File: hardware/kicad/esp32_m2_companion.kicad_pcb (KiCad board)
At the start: 4 copper layers, 22 x 42 mm, 33 parts, among them J1 M2_KEYB_2242_EDGE, J3 Conn_01x04, J4 Conn_01x08, U1 USBLC6-2SC6, U2 ESP32-S3-WROOM-1

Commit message: leds: simple 3D model for the side-view LED (D3); link D3/D4 to their library
- 3dmodels/LED_TJ-S1706_SideView.wrl: 1.70x0.60x1.10 mm body, lens on
  the emitting face, end terminals (renders showed bare pads).
- D3/D4 board instances had no library nickname, so DRC library parity
  never checked them (corrects an earlier claim, see findings). Linked
  to esp32_m2_companion:LED_TJ-S1706_SideView; parity passes.

make drc: 0 violations, 0 unconnected.

Co-Authored-By: Claude Opus 5.5 <noreply@anthropic.com>
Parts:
- D3, D4: footprint LED_TJ-S1706_SideView -> esp32_m2_companion:LED_TJ-S1706_SideView
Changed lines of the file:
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@@
 		)
 	)
-	(footprint "LED_TJ-S1706_SideView"
+	(footprint "esp32_m2_companion:LED_TJ-S1706_SideView"
 		(layer "B.Cu")
 		(at 90.2 126.4 90)
@@
 		)
 		(embedded_fonts no)
+		(model "${KIPRJMOD}/3dmodels/LED_TJ-S1706_SideView.wrl"
+			(offset
+				(xyz 0 0 0)
+			)
+			(scale
+				(xyz 1 1 1)
+			)
+			(rotate
+				(xyz 0 0 0)
+			)
+		)
 	)
 	(footprint "TestPoint:TestPoint_Pad_D1.5mm"
@@
 		(embedded_fonts no)
 	)
-	(footprint "LED_TJ-S1706_SideView"
+	(footprint "esp32_m2_companion:LED_TJ-S1706_SideView"
 		(layer "B.Cu")
 		(at 90.2 129.8 90)
@@
 		)
 		(embedded_fonts no)
+		(model "${KIPRJMOD}/3dmodels/LED_TJ-S1706_SideView.wrl"
+			(offset
+				(xyz 0 0 0)
+			)
+			(scale
+				(xyz 1 1 1)
+			)
+			(rotate
+				(xyz 0 0 0)
+			)
+		)
 	)
 	(footprint "Resistor_SMD:R_0603_1608Metric"

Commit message: v2 GATE V3 (wip): RPW eFuse footprint, netlist->board sync keeping rev-B routing
- tools/gen_fp_rpw.py: TI RPW0010A footprint from tps25947.pdf drawing
  4225183/A (land p.73, stencil p.74: split paste on IN/OUT, L-pads as
  two rects per pin), NSMD 0.05 mm.
- tools/v2_sync_pcb.py: KiCad-9 headless 'update PCB from netlist' in two
  processes (remove changed footprints; add new ones parked off-card and
  assign every pad net from the netlist). Applied: FB1 0805->0603, 31 new
  footprints, 167 pad nets set, no existing net changed.

Co-Authored-By: Claude Opus 5.5 <noreply@anthropic.com>
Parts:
- added C10: 100nF 50V, Capacitor_SMD:C_0603_1608Metric, F.Cu at (118.0, 108.0)
- added C11: 100nF 50V, Capacitor_SMD:C_0603_1608Metric, F.Cu at (118.0, 111.0)
- added C12: 100nF 50V, Capacitor_SMD:C_0603_1608Metric, F.Cu at (118.0, 114.0)
- added C13: 1uF 50V, Capacitor_SMD:C_0603_1608Metric, F.Cu at (118.0, 117.0)
- added C14: 100nF 50V, Capacitor_SMD:C_0603_1608Metric, F.Cu at (118.0, 120.0)
- added Q1: SSM6N56FE, Package_TO_SOT_SMD:SOT-563, F.Cu at (118.0, 126.0)
- added Q2: SSM6N56FE, Package_TO_SOT_SMD:SOT-563, F.Cu at (118.0, 129.0)
- added Q3: SSM6N56FE, Package_TO_SOT_SMD:SOT-563, F.Cu at (118.0, 132.0)
- added R20: 4k7, Resistor_SMD:R_0402_1005Metric, F.Cu at (118.0, 135.0)
- added R21: 4k7, Resistor_SMD:R_0402_1005Metric, F.Cu at (118.0, 138.0)
- added R22: 1M, Resistor_SMD:R_0402_1005Metric, F.Cu at (118.0, 141.0)
- added R23: 1M, Resistor_SMD:R_0402_1005Metric, F.Cu at (118.0, 144.0)
- added R24: 100k, Resistor_SMD:R_0402_1005Metric, F.Cu at (118.0, 147.0)
- added R25: 100k, Resistor_SMD:R_0402_1005Metric, F.Cu at (118.0, 150.0)
- added R26: 10k, Resistor_SMD:R_0603_1608Metric, F.Cu at (118.0, 153.0)
- added R27: 100k, Resistor_SMD:R_0402_1005Metric, F.Cu at (118.0, 156.0)
- added R28: 100k, Resistor_SMD:R_0402_1005Metric, F.Cu at (118.0, 159.0)
- added R29: 1M, Resistor_SMD:R_0402_1005Metric, F.Cu at (118.0, 162.0)
- added R30: 10k, Resistor_SMD:R_0603_1608Metric, F.Cu at (118.0, 165.0)
- added R31: 100k 0.1%, Resistor_SMD:R_0402_1005Metric, F.Cu at (118.0, 168.0)
- added R32: 52.3k 0.1%, Resistor_SMD:R_0402_1005Metric, F.Cu at (118.0, 171.0)
- added R33: 1M, Resistor_SMD:R_0402_1005Metric, F.Cu at (118.0, 174.0)
- added R34: 3.3k, Resistor_SMD:R_0402_1005Metric, F.Cu at (118.0, 177.0)
- added RN1: 220R, Resistor_SMD:R_Array_Convex_4x0402, F.Cu at (118.0, 180.0)
- added RN2: 220R, Resistor_SMD:R_Array_Convex_4x0402, F.Cu at (118.0, 183.0)
- added RN3: 220R, Resistor_SMD:R_Array_Convex_4x0402, F.Cu at (118.0, 186.0)
- added U3: TMUX1511_RSV, Package_DFN_QFN:UQFN-16_1.8x2.6mm_P0.4mm, F.Cu at (118.0, 189.0)
- added U4: TMUX1511_RSV, Package_DFN_QFN:UQFN-16_1.8x2.6mm_P0.4mm, F.Cu at (118.0, 192.0)
- added U5: TMUX1511_RSV, Package_DFN_QFN:UQFN-16_1.8x2.6mm_P0.4mm, F.Cu at (118.0, 195.0)
- added U6: TPS259470A_RPW, esp32_m2_companion:TI_RPW_VQFN-10_2x2mm_P0.5mm, F.Cu at (118.0, 198.0)
- FB1: value 100R@100MHz 800mA -> 120R@100MHz 2A; footprint Inductor_SMD:L_0805_2012Metric -> Inductor_SMD:L_0603_1608Metric; moved to F.Cu
- moved FB1 33.5 mm to (118.0, 123.0), turned to 0 degrees
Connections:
- FB1 pad 1: +3V3_M2 -> +3V3_EFUSE
- J1 pad 1: (no net) -> CONFIG_3
- J1 pad 10: (no net) -> LED_1_n
- J1 pad 21: (no net) -> GND
- J1 pad 23: (no net) -> WAKE_ON_WWAN_n
- J1 pad 26: (no net) -> W_DISABLE2_n
- J1 pad 30: (no net) -> EXP_0
- J1 pad 32: (no net) -> EXP_1
- J1 pad 34: (no net) -> EXP_2
- J1 pad 36: (no net) -> EXP_3
- J1 pad 40: (no net) -> EXP_4
- J1 pad 59: (no net) -> EXP_5
- J1 pad 60: (no net) -> EXP_6
- J1 pad 61: (no net) -> EXP_7
- J1 pad 62: (no net) -> EXP_8
- J1 pad 63: (no net) -> EXP_9
- J1 pad 64: (no net) -> EXP_10
- J1 pad 65: (no net) -> EXP_11
- J1 pad 69: (no net) -> GND
- J1 pad 75: (no net) -> CONFIG_2
- U2 pad 10: (no net) -> IO17
- U2 pad 11: (no net) -> IO18
- U2 pad 24: (no net) -> IO47
- U2 pad 31: (no net) -> EXP_OE
- U2 pad 32: (no net) -> IO39
- U2 pad 33: (no net) -> IO40
- U2 pad 34: (no net) -> IO41
- U2 pad 35: (no net) -> IO42
- U2 pad 38: (no net) -> IO2
- U2 pad 39: (no net) -> IO1
- U2 pad 4: (no net) -> IO4
- U2 pad 5: (no net) -> IO5
- U2 pad 6: (no net) -> IO6
- U2 pad 7: (no net) -> IO7
- U2 pad 8: (no net) -> IO15
- U2 pad 9: (no net) -> IO16

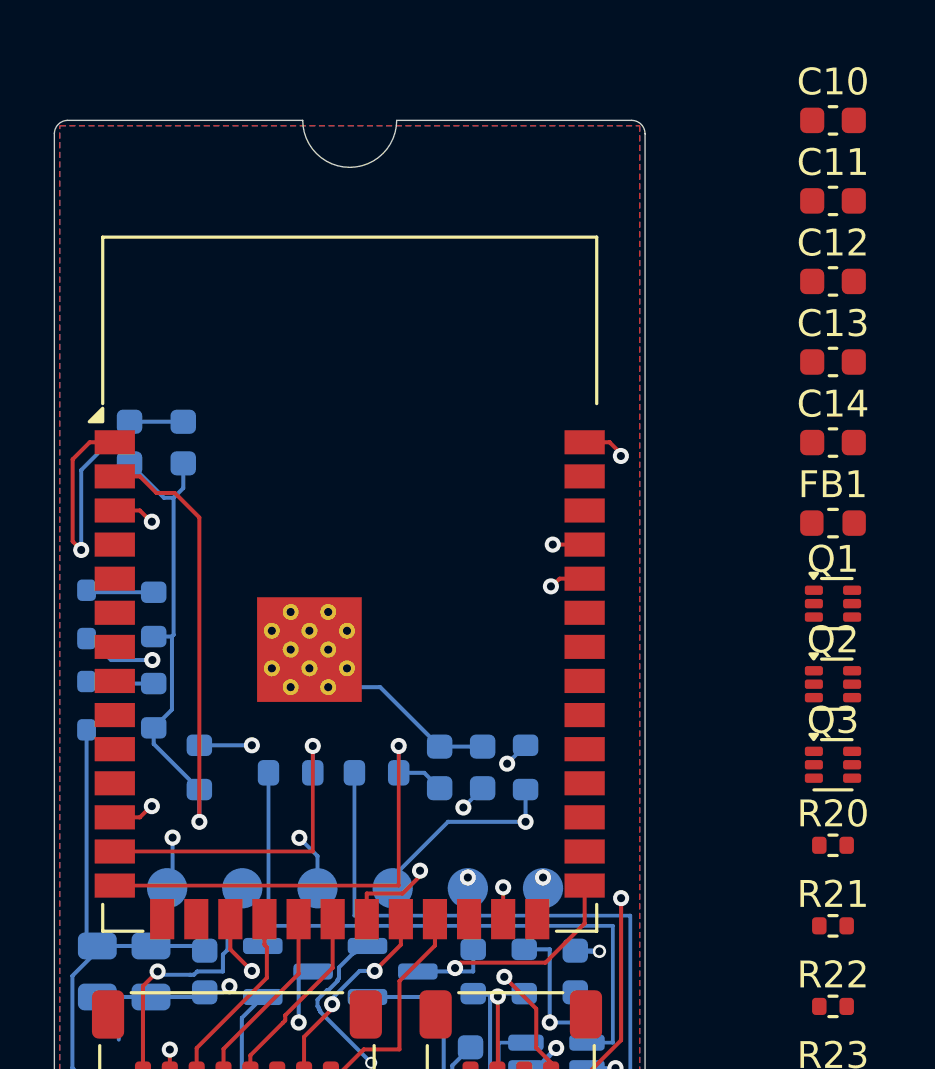
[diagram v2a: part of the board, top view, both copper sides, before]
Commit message: v2 GATE V3 (wip): drop TP3-TP6, TP1/TP2 1.0 mm (owner decision)
TXD0/RXD0/3V3/GND test points duplicated J4/J3 pins; the row blocked the
module<->finger band. v2_sync_pcb stage1 now also removes footprints that
left the netlist. ERC + contract netlist check PASS; review PDF/BOM updated.

Co-Authored-By: Claude Opus 5.5 <noreply@anthropic.com>
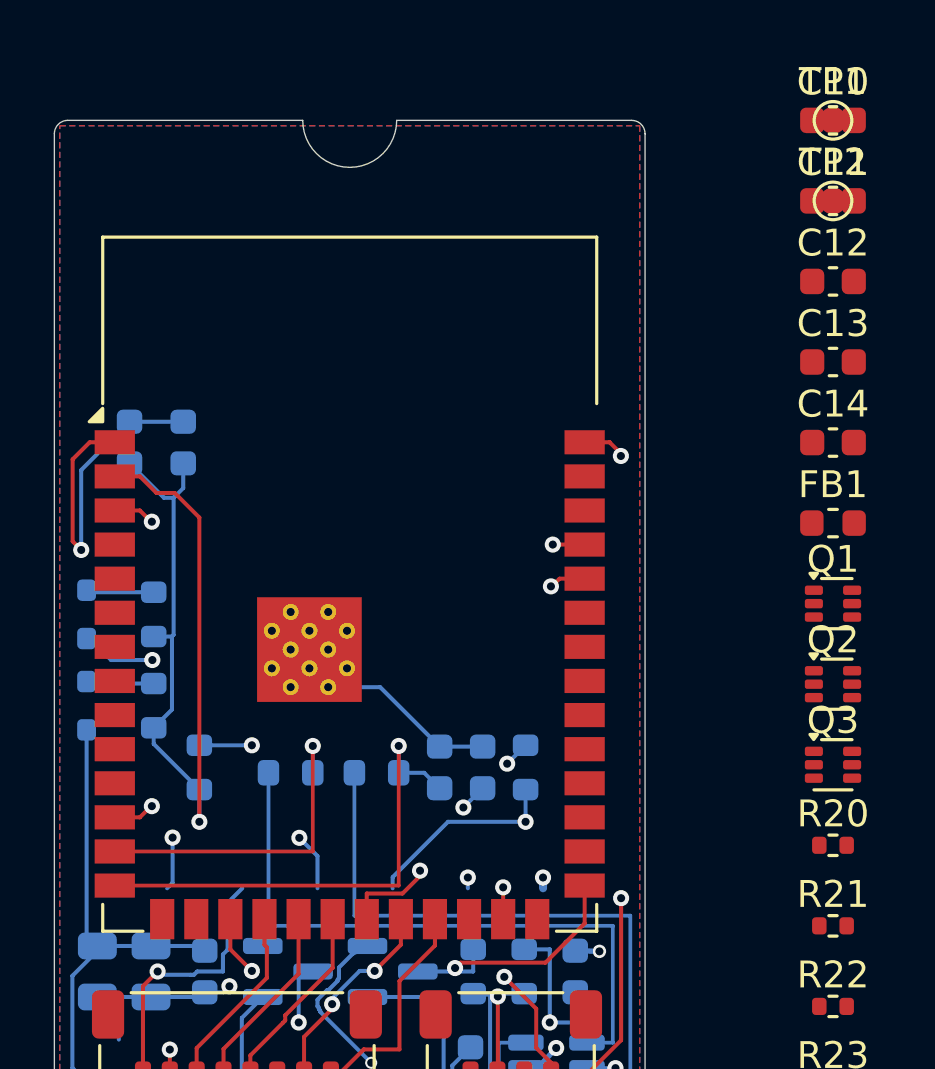
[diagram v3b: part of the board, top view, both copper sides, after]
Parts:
- removed TP3: TP_TXD0, TestPoint:TestPoint_Pad_D1.5mm
- removed TP4: TP_RXD0, TestPoint:TestPoint_Pad_D1.5mm
- removed TP5: TP_3V3, TestPoint:TestPoint_Pad_D1.5mm
- removed TP6: TP_GND, TestPoint:TestPoint_Pad_D1.5mm
- TP1, TP2: footprint TestPoint:TestPoint_Pad_D1.5mm -> TestPoint:TestPoint_Pad_D1.0mm; moved to F.Cu
- moved TP2 35.6 mm to (118.0, 111.0)
- moved TP1 30.6 mm to (118.0, 108.0)

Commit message: v2 GATE V3 (wip): 6 layers (JLC06081H-2116), +3V3 plane In2->In4, USB 0.15/0.13
tools/v2_to_6layer.py: copper count 6, rev-B In2 plane + 18 tracks moved to
In4 (L5 PWR), In2/In3 free for signals, all-layer rule areas extended.
No new DRC issue among rev-B items. docs/stackup.md v2 section; USB_DIFF
net class 0.15/0.13 (89.6 ohm); rev-B pair kept (~92 ohm, within 10 %).

Co-Authored-By: Claude Opus 5.5 <noreply@anthropic.com>
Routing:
- added copper zone on In4.Cu, net +3V3
- removed copper zone on In2.Cu, net +3V3
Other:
- copper layers 4 -> 6
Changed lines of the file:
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@@
 		(4 "In1.Cu" signal)
 		(6 "In2.Cu" signal)
+		(8 "In3.Cu" signal)
+		(10 "In4.Cu" signal)
 		(2 "B.Cu" signal)
 		(9 "F.Adhes" user "F.Adhesive")
@@
 		(end 109.9 137.475)
 		(width 0.15)
-		(layer "In2.Cu")
+		(layer "In4.Cu")
 		(net 1)
 	)
@@
 		(end 106.55 134.125)
 		(width 0.15)
-		(layer "In2.Cu")
+		(layer "In4.Cu")
 		(net 1)
 	)
@@
 		(width 0.3)
 		(locked yes)
-		(layer "In2.Cu")
+		(layer "In4.Cu")
 		(net 2)
 	)
@@
 		(width 0.15)
 		(locked yes)
-		(layer "In2.Cu")
+		(layer "In4.Cu")
 		(net 3)
 	)
@@
 		(width 0.15)
 		(locked yes)
-		(layer "In2.Cu")
+		(layer "In4.Cu")
 		(net 3)
 	)
@@
 		(width 0.15)
 		(locked yes)
-		(layer "In2.Cu")
+		(layer "In4.Cu")
 		(net 3)
 	)
@@
 		(end 99.9 131.7)
 		(width 0.15)
-		(layer "In2.Cu")
+		(layer "In4.Cu")
 		(net 4)
 	)
@@
 		(end 90.3 124.3)
 		(width 0.15)
-		(layer "In2.Cu")
+		(layer "In4.Cu")
 		(net 4)
 	)
@@
 		(end 90.3 145.4)
 		(width 0.15)
-		(layer "In2.Cu")
+		(layer "In4.Cu")
 		(net 4)
 	)
@@
 		(end 104.4 136.2)
 		(width 0.15)
-		(layer "In2.Cu")
+		(layer "In4.Cu")
 		(net 4)
 	)
@@
 		(end 102.6194 135.9456)
 		(width 0.15)
-		(layer "In2.Cu")
+		(layer "In4.Cu")
 		(net 9)
 	)
@@
 		(end 97.3 141.265)
 		(width 0.15)
-		(layer "In2.Cu")
+		(layer "In4.Cu")
 		(net 9)
 	)
@@
 		(end 110.1077 136.9691)
 		(width 0.15)
-		(layer "In2.Cu")
+		(layer "In4.Cu")
 		(net 12)
 	)
@@
 		(end 110.1077 136.2039)
 		(width 0.15)
-		(layer "In2.Cu")
+		(layer "In4.Cu")
 		(net 12)
 	)
@@
 		(end 96.356 131.275)
 		(width 0.15)
-		(layer "In2.Cu")
+		(layer "In4.Cu")
 		(net 13)
 	)
@@
 		(end 98.1232 134.722)
 		(width 0.15)
-		(layer "In2.Cu")
+		(layer "In4.Cu")
 		(net 19)
 	)
@@
 		(end 94.2471 142.6078)
 		(width 0.15)
-		(layer "In2.Cu")
+		(layer "In4.Cu")
 		(net 19)
 	)
@@
 		(end 98.1232 138.7317)
 		(width 0.15)
-		(layer "In2.Cu")
+		(layer "In4.Cu")
 		(net 19)
 	)
@@
 		(net 0)
 		(net_name "")
-		(layers "F.Cu" "B.Cu" "In1.Cu" "In2.Cu")
+		(layers "F.Cu" "B.Cu" "In1.Cu" "In2.Cu" "In3.Cu" "In4.Cu")
 		(name "antenna_keepout_espressif_hdg")
 		(hatch edge 0.5)
@@
 		(net 1)
 		(net_name "+3V3")
-		(layer "In2.Cu")
-		(name "PWR_L3")
+		(layer "In4.Cu")
+		(name "PWR_L5")
 		(hatch edge 0.5)
 		(connect_pads yes
@@
 		(min_thickness 0.15)
 		(filled_areas_thickness no)
-		(fill yes
+		(fill
 			(thermal_gap 0.25)
 			(thermal_bridge_width 0.3)

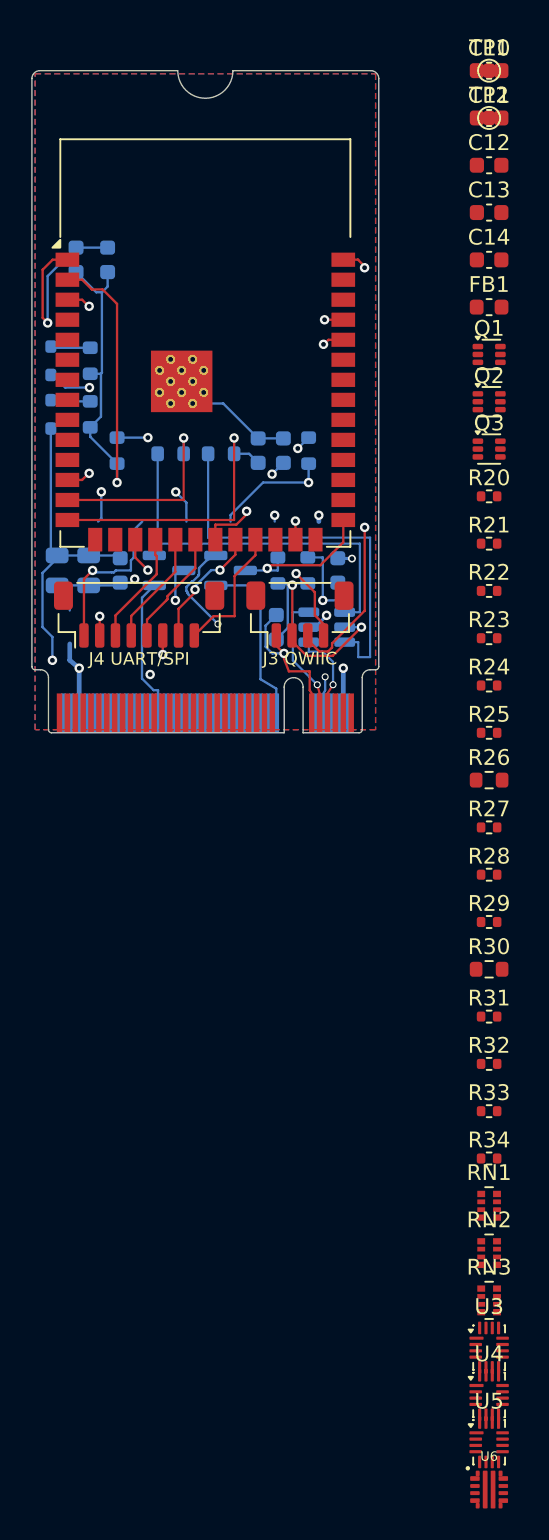
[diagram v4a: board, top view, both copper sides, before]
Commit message: v2 GATE V3 (wip): rip up rev-B routing (USB pair kept), place v2 parts
- tools/v2_ripup.py: remove all rev-B tracks/vias except the USB nets
  (kept + locked): rev B ran signals on its plane layers.
- tools/v2_place.py: v2 parts to the nearest legal bottom-side spot of
  routing-aware targets (switches above their fingers, arrays at the module
  pads, eFuse at the power entry, detect + host cells under the module).
  All 33 placed.

Co-Authored-By: Claude Opus 5.5 <noreply@anthropic.com>
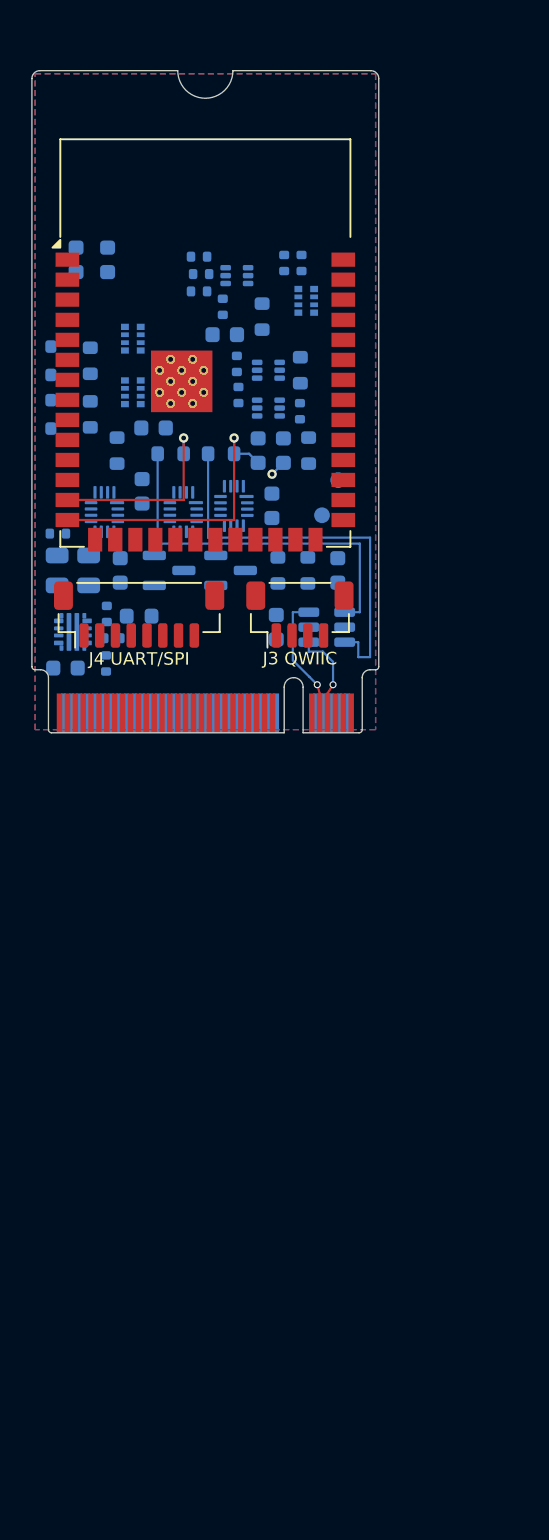
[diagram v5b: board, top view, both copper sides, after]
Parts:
- C10, C11, C12, C13, C14, FB1, Q1, Q2, Q3, R20, R21, R22, R23, R24, R25, R26, R27, R28, R29, R30, R31, R32, R33, R34, RN1, RN2, RN3, TP1, TP2, U3, U4, U5, U6: moved to B.Cu
- moved RN2 62.2 mm to (95.4, 125.0), turned to 180 degrees
- moved U5 62.1 mm to (98.6, 136.0), turned to 180 degrees
- moved RN3 61.9 mm to (95.4, 128.4), turned to 180 degrees
- moved U4 61.1 mm to (93.6, 136.0), turned to 180 degrees
- moved U6 60.5 mm to (91.6, 143.6), turned to 180 degrees
- moved RN1 58.6 mm to (106.4, 122.6), turned to 180 degrees
- moved U3 55.8 mm to (101.8, 135.6), turned to 180 degrees
- moved R33 45.7 mm to (90.6, 137.4)
- moved R30 39.8 mm to (106.0, 127.0), turned to 90 degrees
- moved R34 39.7 mm to (93.7, 145.6), turned to 90 degrees
- moved C14 37.3 mm to (91.1, 145.9)
- moved R32 36.1 mm to (94.1, 144.0)
- moved R31 35.2 mm to (93.8, 142.5), turned to 90 degrees
- moved R29 34.6 mm to (106.0, 129.6), turned to 90 degrees
- moved R28 34.3 mm to (102.1, 128.6), turned to 90 degrees
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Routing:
- net GND: track 133.4 -> 0.00 mm, vias 7 -> 0
- net +3V3: track 95.2 -> 0.00 mm, vias 5 -> 0
- net EN: track 49.1 -> 0.00 mm, vias 4 -> 0
- net TXD0: track 44.5 -> 0.00 mm, vias 2 -> 0
- net IO8: track 42.2 -> 0.00 mm, vias 3 -> 0
- net +3V3_M2: track 32.1 -> 0.00 mm, vias 3 -> 0
- net RXD0: track 30.6 -> 0.00 mm, vias 3 -> 0
- net IO0: track 27.7 -> 0.00 mm, vias 2 -> 0
- net IO9: track 27.3 -> 0.00 mm, vias 3 -> 0
- net LED_STATUS_n: track 22.1 -> 0.00 mm, vias 2 -> 0
- net W_DISABLE1_n: track 16.6 -> 0.00 mm, vias 2 -> 0
- net IO13: track 15.9 -> 0.00 mm, vias 2 -> 0
- net PCIE_1_GPIO_5: track 11.5 -> 0.00 mm
- net PERST_n: track 9.01 -> 0.00 mm
- net IO21: track 8.46 -> 0.00 mm
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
